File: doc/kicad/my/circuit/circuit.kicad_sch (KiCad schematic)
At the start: 13 parts, among them J1 Analog, J10 PCF8574 I²C Socket, J2 Digital, J3 4x4 Button Matrix, J4 Joystick, J5 Pedals, J6 Handbrake, J7 Encoder, J8 LCD Socket, J9 PCF8574 LCD Socekt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

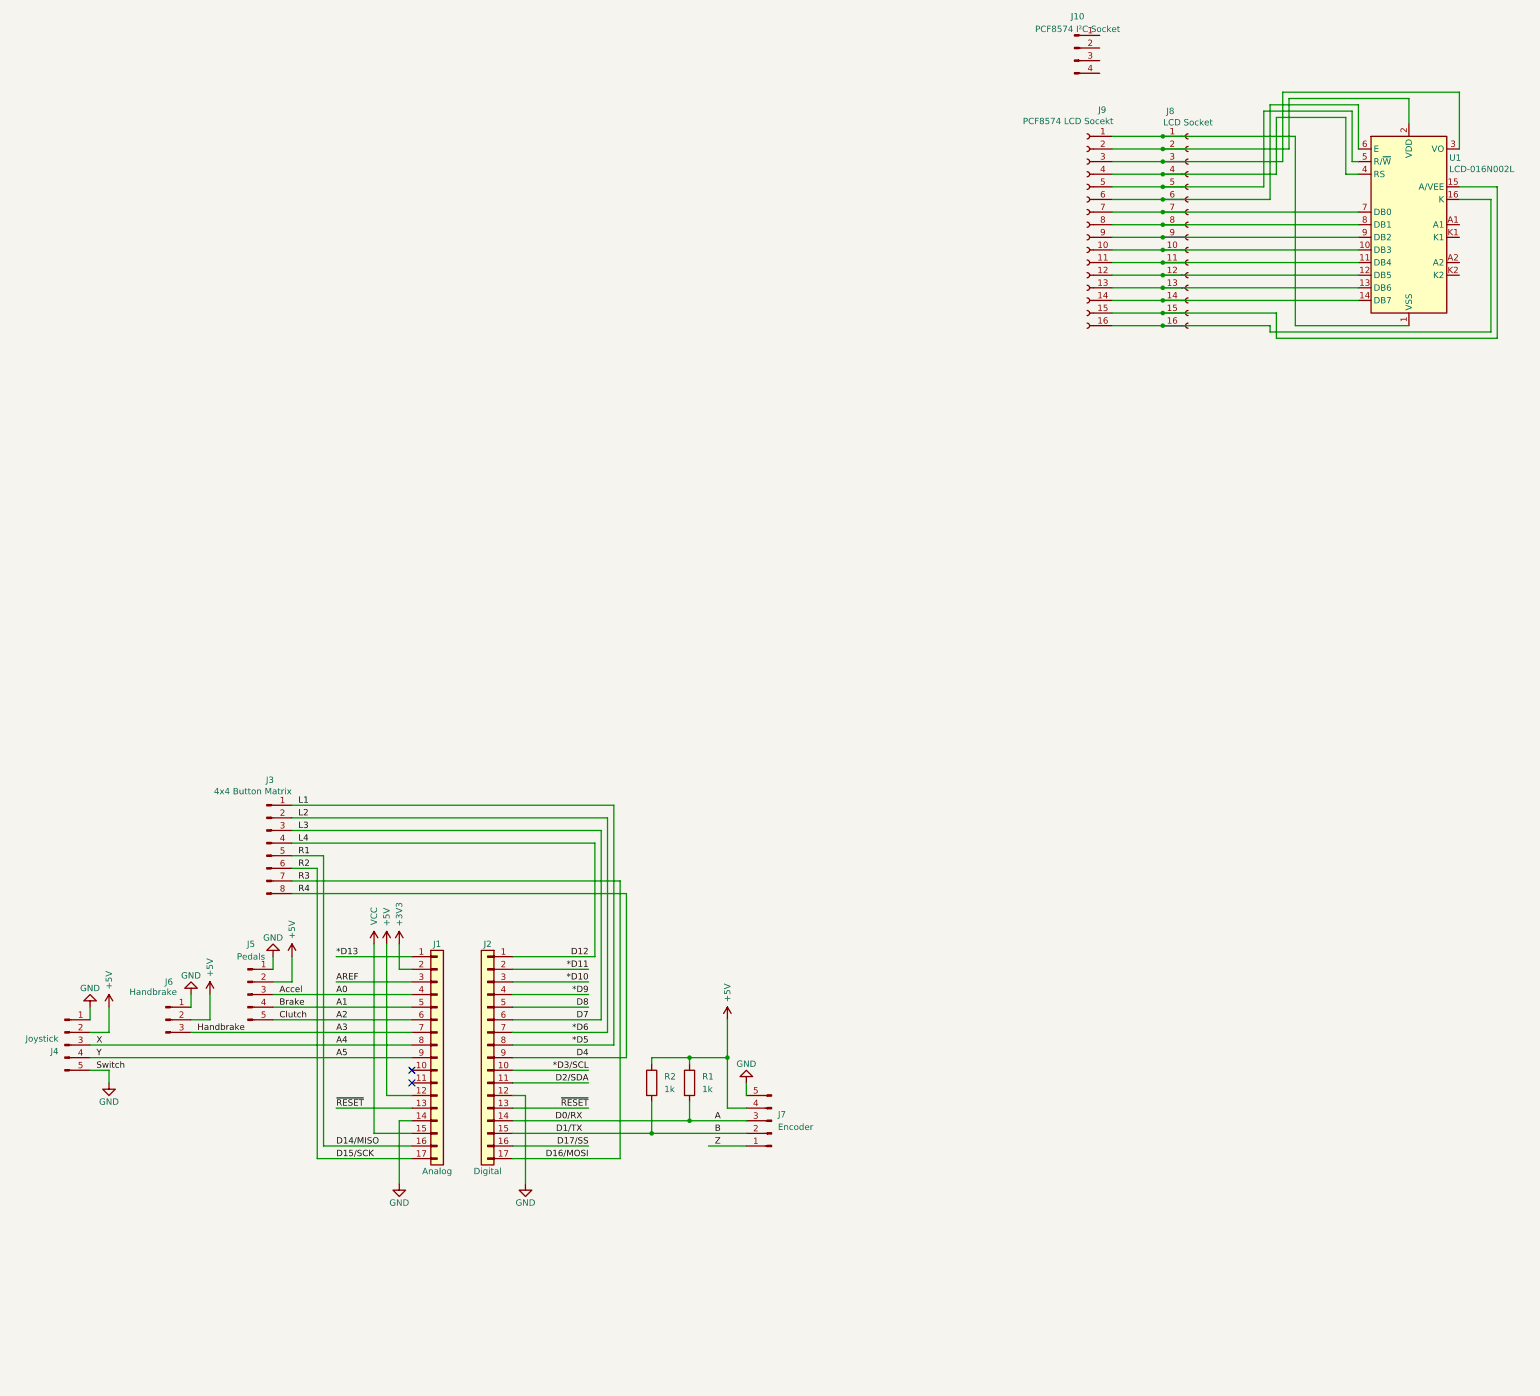
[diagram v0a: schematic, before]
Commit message: add display class
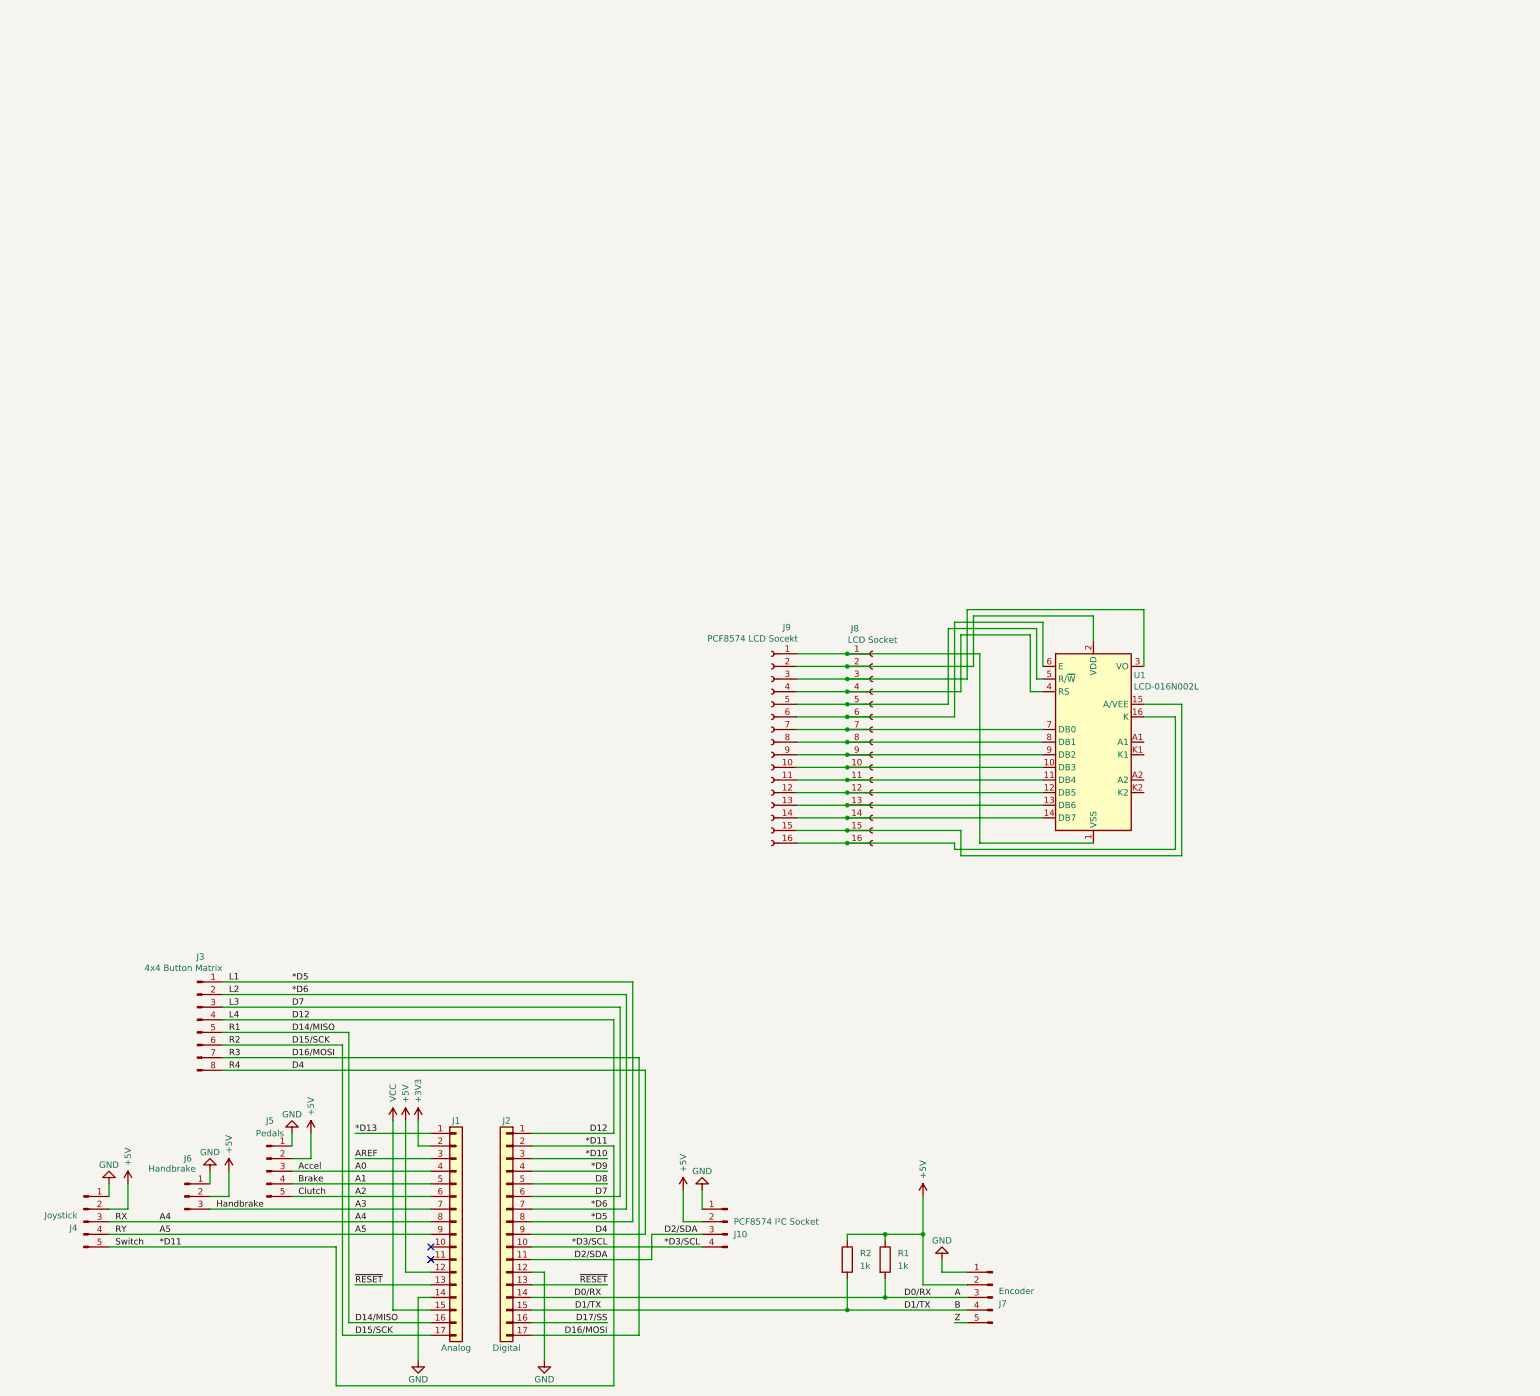
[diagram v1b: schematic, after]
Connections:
- net *D11: now also J4.5 (Pin_5)
- net *D3/SCL: now also J10.4 (Pin_4)
- net +5V: now also J10.2 (Pin_2), J7.2 (Pin_2); no longer J7.4 (Pin_4)
- net B: now also J7.4 (Pin_4); no longer J7.2 (Pin_2)
- net D2/SDA: now also J10.3 (Pin_3)
- net GND: now also J10.1 (Pin_1), J7.1 (Pin_1); no longer J4.5 (Pin_5), J7.5 (Pin_5)
- net Z: now also J7.5 (Pin_5); no longer J7.1 (Pin_1)
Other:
- moved on the sheet: J1, J10, J2, J3, J4, J5, J6, J7, J8, J9, R1, R2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
